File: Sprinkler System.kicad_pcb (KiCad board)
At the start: 2 copper layers, 165 x 85 mm, 74 parts, among them J1 Main Supply, J2 XFMR_Out, J20 Station_0, J21 Station_1, J22 Station_2, J23 Station_3, J24 Station_4, J25 Station_5, J3 XFMR_In, J4 Conn_Button, J5 UART0, J6 I2C, K1 G3MB-202P, K20 G5LE-1-DC5, K21 G5LE-1-DC5, K22 G5LE-1-DC5, K23 G5LE-1-DC5, K24 G5LE-1-DC5, K25 G5LE-1-DC5, SW1 EN, SW2 BOOT, U1 AMS1117-3.3, U2 EL817, U3 HLK-PM01, U4 ESP32-WROOM-32U, U5 ULN2803A

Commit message: Replace J1 mains connector with 5.08mm MSTBA (250V rated)
The previous Phoenix MC 1,5/3-G-3.81 connector is only rated 160V and
its 3.81mm pitch leaves just 2.0mm Live-to-Earth creepage at 240VAC.
Swap to MSTBA 2,5/3-G-5,08 (project-lib copy with silkscreen clipped at
the board edge), shift J1 up 2.5mm so the deeper body stays flush with
the edge, re-route the L_Supply/Neut/GND stubs, move the E/L/N labels
to the new pad pitch, and reshape the mains demarcation silk line and
the 24V_Comm corner to preserve >=3mm mains-to-SELV spacing.

ERC/DRC: 0 violations.

Co-Authored-By: Claude Fable 5 <noreply@anthropic.com>
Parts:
- J1: footprint Connector_Phoenix_MC:PhoenixContact_MC_1,5_3-G-3.81_1x03_P3.81mm_Horizontal -> Sprinkler System:PhoenixContact_MSTBA_2,5_3-G-5,08_1x03_P5.08mm_Horizontal_EdgeClip
- moved J1 2.50 mm to (82.0, 120.5)
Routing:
- net GND: track 132.1 -> 129.6 mm
- net L_Supply: track 26.7 -> 24.7 mm
- net Neut: track 56.3 -> 58.0 mm
- net 24V_Comm: track 237.0 -> 236.1 mm
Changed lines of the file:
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@@
 		)
 	)
-	(footprint "Connector_Phoenix_MC:PhoenixContact_MC_1,5_3-G-3.81_1x03_P3.81mm_Horizontal"
+	(footprint "Sprinkler System:PhoenixContact_MSTBA_2,5_3-G-5,08_1x03_P5.08mm_Horizontal_EdgeClip"
 		(layer "F.Cu")
-		(at 82 123)
-		(descr "Generic Phoenix Contact connector footprint for: MC_1,5/3-G-3.81; number of pins: 03; pin pitch: 3.81mm; Angled || order number: 1803280 8A 160V")
-		(tags "phoenix_contact connector MC_01x03_G_3.81mm")
+		(at 82 120.5)
+		(descr "Generic Phoenix Contact connector footprint for: MSTBA_2,5/3-G-5,08; number of pins: 03; pin pitch: 5.08mm; Angled || order number: 1757255 12A || order number: 1923872 16A (HC)")
+		(tags "phoenix_contact connector MSTBA_01x03_G_5.08mm")
 		(property "Reference" "J1"
-			(at 11.375 5.27 90)
+			(at -2.5 -4.3 0)
 			(layer "F.SilkS")
 			(effects
@@
 		)
 		(property "Value" "Main Supply"
-			(at -4.5 2.73 90)
-			(layer "F.SilkS")
+			(at 5.08 12.2 0)
+			(layer "F.Fab")
 			(effects
 				(font
@@
 		(duplicate_pad_numbers_are_jumpers no)
 		(fp_line
-			(start -2.71 -1.31)
-			(end -2.71 8.11)
+			(start -1 9.7)
+			(end 1 9.7)
+			(stroke
+				(width 0.12)
+				(type solid)
+			)
+			(layer "F.SilkS")
+		)
+		(fp_line
+			(start -0.75 8.61)
+			(end -1 9.7)
 			(stroke
 				(width 0.12)
@@
 		)
 		(fp_line
-			(start -2.71 -1.31)
-			(end -1.05 -1.31)
+			(start -0.3 -2.91)
+			(end 0.3 -2.91)
 			(stroke
 				(width 0.12)
@@
 		)
 		(fp_line
-			(start -2.71 4.8)
-			(end 10.33 4.8)
+			(start 0 -2.31)
+			(end -0.3 -2.91)
 			(stroke
 				(width 0.12)
@@
 		)
 		(fp_line
-			(start -2.71 8.11)
-			(end 10.33 8.11)
+			(start 0.3 -2.91)
+			(end 0 -2.31)
 			(stroke
 				(width 0.12)
@@
 		)
 		(fp_line
-			(start -0.3 -2.6)
-			(end 0.3 -2.6)
+			(start 0.75 8.61)
+			(end -0.75 8.61)
 			(stroke
 				(width 0.12)
@@
 		)
 		(fp_line
-			(start 0 -2)
-			(end -0.3 -2.6)
+			(start 1 9.7)
+			(end 0.75 8.61)
 			(stroke
 				(width 0.12)
@@
 		)
 		(fp_line
-			(start 0.3 -2.6)
-			(end 0 -2)
+			(start 4.08 9.7)
+			(end 6.08 9.7)
 			(stroke
 				(width 0.12)
@@
 		)
 		(fp_line
-			(start 1.05 -1.31)
-			(end 2.76 -1.31)
+			(start 4.33 8.61)
+			(end 4.08 9.7)
 			(stroke
 				(width 0.12)
@@
 		)
 		(fp_line
-			(start 4.86 -1.31)
-			(end 6.57 -1.31)
+			(start 5.83 8.61)
+			(end 4.33 8.61)
 			(stroke
 				(width 0.12)
@@
 		)
 		(fp_line
-			(start 10.33 -1.31)
-			(end 8.67 -1.31)
+			(start 6.08 9.7)
+			(end 5.83 8.61)
 			(stroke
 				(width 0.12)
@@
 		)
 		(fp_line
-			(start 10.33 8.11)
-			(end 10.33 -1.31)
+			(start 9.16 9.7)
+			(end 11.16 9.7)
+			(stroke
+				(width 0.12)
+				(type solid)
+			)
+			(layer "F.SilkS")
+		)
+		(fp_line
+			(start 9.41 8.61)
+			(end 9.16 9.7)
+			(stroke
+				(width 0.12)
+				(type solid)
+			)
+			(layer "F.SilkS")
+		)
+		(fp_line
+			(start 10.91 8.61)
+			(end 9.41 8.61)
+			(stroke
+				(width 0.12)
+				(type solid)
+			)
+			(layer "F.SilkS")
+		)
+		(fp_line
+			(start 11.16 9.7)
+			(end 10.91 8.61)
+			(stroke
+				(width 0.12)
+				(type solid)
+			)
+			(layer "F.SilkS")
+		)
+		(fp_rect
+			(start -3.65 -2.11)
+			(end 13.81 9.7)
 			(stroke
 				(width 0.12)
 				(type solid)
 			)
+			(fill no)
+			(layer "F.SilkS")
+		)
+		(fp_rect
+			(start -3.65 6.81)
+			(end 13.81 8.61)
+			(stroke
+				(width 0.12)
+				(type solid)
+			)
+			(fill no)
 			(layer "F.SilkS")
 		)
 		(fp_rect
-			(start -3.21 -2.3)
-			(end 10.72 8.5)
+			(start -4.04 -2.5)
+			(end 14.21 10.5)
 			(stroke
 				(width 0.05)
@@
 		)
 		(fp_line
-			(start 0 0)
-			(end -0.8 -1.2)
+			(start 0 -0.5)
+			(end -0.95 -2)
 			(stroke
 				(width 0.1)
@@
 		)
 		(fp_line
-			(start 0.8 -1.2)
-			(end 0 0)
+			(start 0.95 -2)
+			(end 0 -0.5)
 			(stroke
 				(width 0.1)
@@
 		)
 		(fp_rect
-			(start -2.6 -1.2)
-			(end 10.22 8)
+			(start -3.54 -2)
+			(end 13.7 10)
 			(stroke
 				(width 0.1)
@@
 		)
 		(fp_text user "${REFERENCE}"
-			(at 3.81 -0.5 0)
+			(at 5.08 -1.3 0)
 			(layer "F.Fab")
 			(effects
@@
 		(pad "1" thru_hole roundrect
 			(at 0 0)
-			(size 1.8 3.6)
-			(drill 1.2)
+			(size 2.08 3.6)
+			(drill 1.4)
 			(layers "*.Cu" "*.Mask")
 			(remove_unused_layers no)
-			(roundrect_rratio 0.138889)
+			(roundrect_rratio 0.120192)
 			(net "GND")
 			(pinfunction "Pin_1_1")
@@
 		)
 		(pad "2" thru_hole oval
-			(at 3.81 0)
-			(size 1.8 3.6)
-			(drill 1.2)
+			(at 5.08 0)
+			(size 2.08 3.6)
+			(drill 1.4)
 			(layers "*.Cu" "*.Mask")
 			(remove_unused_layers no)
@@
 		)
 		(pad "3" thru_hole oval
-			(at 7.62 0)
-			(size 1.8 3.6)
-			(drill 1.2)
+			(at 10.16 0)
+			(size 2.08 3.6)
+			(drill 1.4)
 			(layers "*.Cu" "*.Mask")
 			(remove_unused_layers no)
@@
 		)
 		(embedded_fonts no)
-		(model "${KICAD10_3DMODEL_DIR}/Connector_Phoenix_MC.3dshapes/PhoenixContact_MC_1,5_3-G-3.81_1x03_P3.81mm_Horizontal.step"
+		(model "${KICAD10_3DMODEL_DIR}/Connector_Phoenix_MSTB.3dshapes/PhoenixContact_MSTBA_2,5_3-G-5,08_1x03_P5.08mm_Horizontal.step"
 			(offset
 				(xyz 0 0 0)
@@
 		(property "Value" "EL817"
 			(at 0 3 0)
-			(layer "F.SilkS")
+			(layer "F.Fab")
 			(effects
 				(font
@@
 	(gr_line
 		(start 92.5 86.5)
-		(end 92.5 119.5)
+		(end 92.5 112)
 		(stroke
 			(width 0.2)
@@
 	)
 	(gr_line
-		(start 92.5 119.5)
-		(end 94.5 121)
+		(start 92.5 112)
+		(end 95.3 114.8)
 		(stroke
 			(width 0.2)
@@
 	)
 	(gr_line
-		(start 94.5 121)
-		(end 94.5 130)
+		(start 95.3 117.4)
+		(end 96.8 117.9)
+		(stroke
+			(width 0.2)
+			(type dash)
+		)
+		(layer "F.SilkS")
+	)
+	(gr_line
+		(start 96.8 117.9)
+		(end 96.8 130)
+		(stroke
+			(width 0.2)
+			(type dash)
+		)
+		(layer "F.SilkS")
+	)
+	(gr_line
+		(start 95.3 114.8)
+		(end 95.3 117.4)
 		(stroke
 			(width 0.2)
@@
 	)
 	(gr_text "E"
-		(at 81.28 120 0)
+		(at 82 117.5 0)
 		(layer "F.SilkS")
 		(effects
@@
 	)
 	(gr_text "L"
-		(at 85.09 120.65 0)
+		(at 87.08 117.5 0)
 		(layer "F.SilkS")
 		(effects
@@
 	)
 	(gr_text "N"
-		(at 89 120.5 0)
+		(at 92.16 117.5 0)
 		(layer "F.SilkS")
 		(effects
@@
 	(segment
 		(start 185 119)
-		(end 97 119)
+		(end 98.5 119)
 		(width 0.6)
 		(layer "B.Cu")
@@
 	)
 	(segment
-		(start 97 119)
-		(end 93 115)
+		(start 98.5 119)
+		(end 93 113.5)
 		(width 0.6)
 		(layer "B.Cu")
@@
 	)
 	(segment
-		(start 93 115)
+		(start 93 113.5)
 		(end 93 85)
 		(width 0.6)
@@
 	(segment
 		(start 82 112)
-		(end 82 123)
+		(end 82 120.5)
 		(width 0.5)
 		(layer "B.Cu")
@@
 	)
 	(segment
-		(start 89.59 122.7975)
-		(end 89.59 118.09)
+		(start 92.16 120.5)
+		(end 92.16 115.57)
 		(width 1)
 		(layer "F.Cu")
@@
 	)
 	(segment
-		(start 89.59 118.09)
-		(end 84.5 113)
+		(start 92.16 115.57)
+		(end 89.59 113)
 		(width 1)
 		(layer "F.Cu")
@@
 	(segment
 		(start 84 116.5)
-		(end 85.81 118.31)
+		(end 87.08 119.58)
 		(width 1)
 		(layer "F.Cu")
@@
 	)
 	(segment
-		(start 85.81 118.31)
-		(end 85.81 123)
+		(start 87.08 119.58)
+		(end 87.08 120.5)
 		(width 1)
 		(layer "F.Cu")
@@
 	)
 	(segment
-		(start 85.78 122.7975)
-		(end 85.7675 122.785)
-		(width 1)
-		(layer "B.Cu")
-		(net "L_Supply")
-	)
-	(segment
 		(start 71 107)
 		(end 71 109.3)
@@
 	)
 	(segment
+		(start 89.59 113)
+		(end 84.5 113)
+		(width 1)
+		(layer "F.Cu")
+		(net "Neut")
+	)
+	(segment

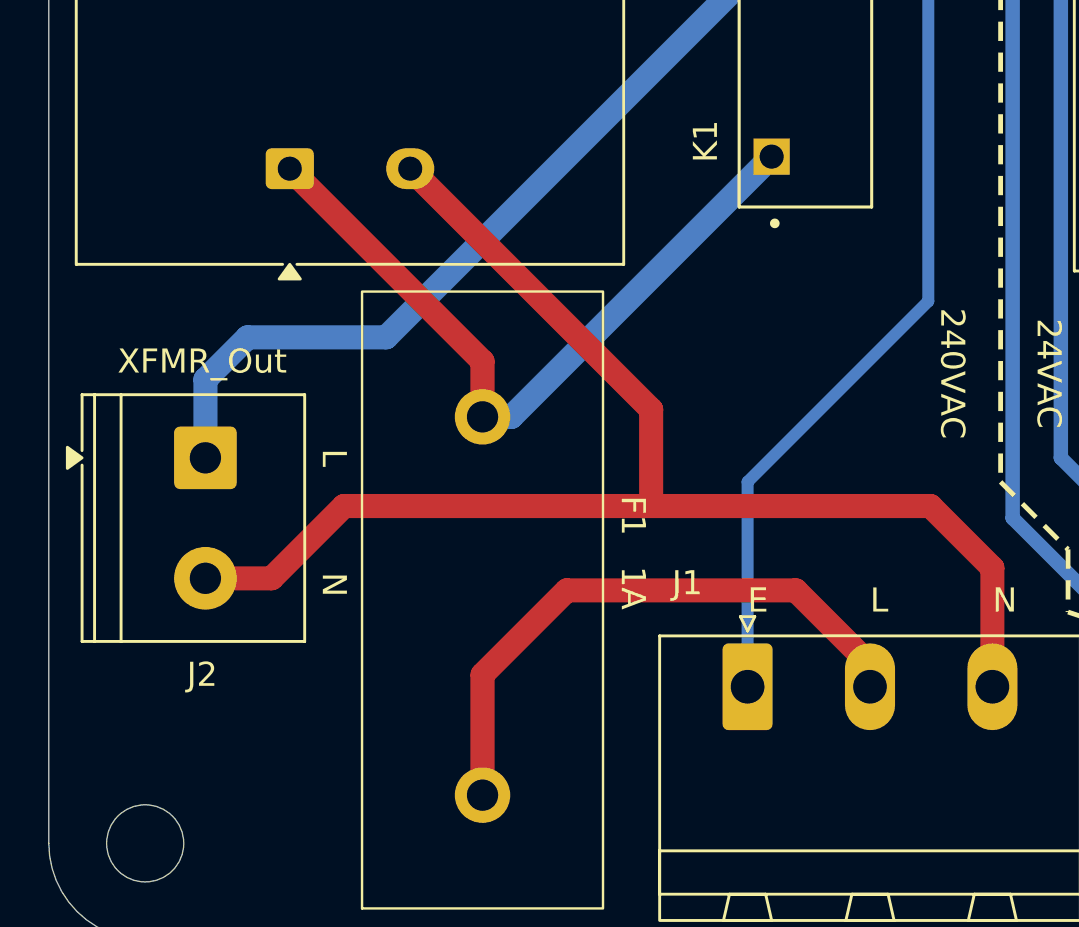
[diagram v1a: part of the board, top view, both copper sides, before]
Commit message: Add 10D471K MOVs: RV1 across transformer primary, RV2 across mains input
The G3MB-202P SSR has a built-in snubber but no overvoltage element;
Omron requires external overvoltage protection for inductive loads.
RV1 (L_SW-Neut) clamps the transformer-primary inductive kick at J2;
RV2 (L-Neut, after F1) provides the HLK-PM01 datasheet-recommended
line surge protection.

Layout: J2 moved up 4.5mm to open space for RV1 below it (clear of the
H3 mounting hole), earth track jogged from x82 to x82.5 to keep >=3mm
from RV2's Neutral pad, J2's L/N silk labels and Reference/Value moved
with it, F1 reference relocated out of RV2's outline. RV1 uses a
project-library footprint copy with silk clipped at the left to clear
the board-margin line.

ERC/DRC: 0 violations. Mains-to-SELV spacing verified >=3mm.

Co-Authored-By: Claude Fable 5 <noreply@anthropic.com>
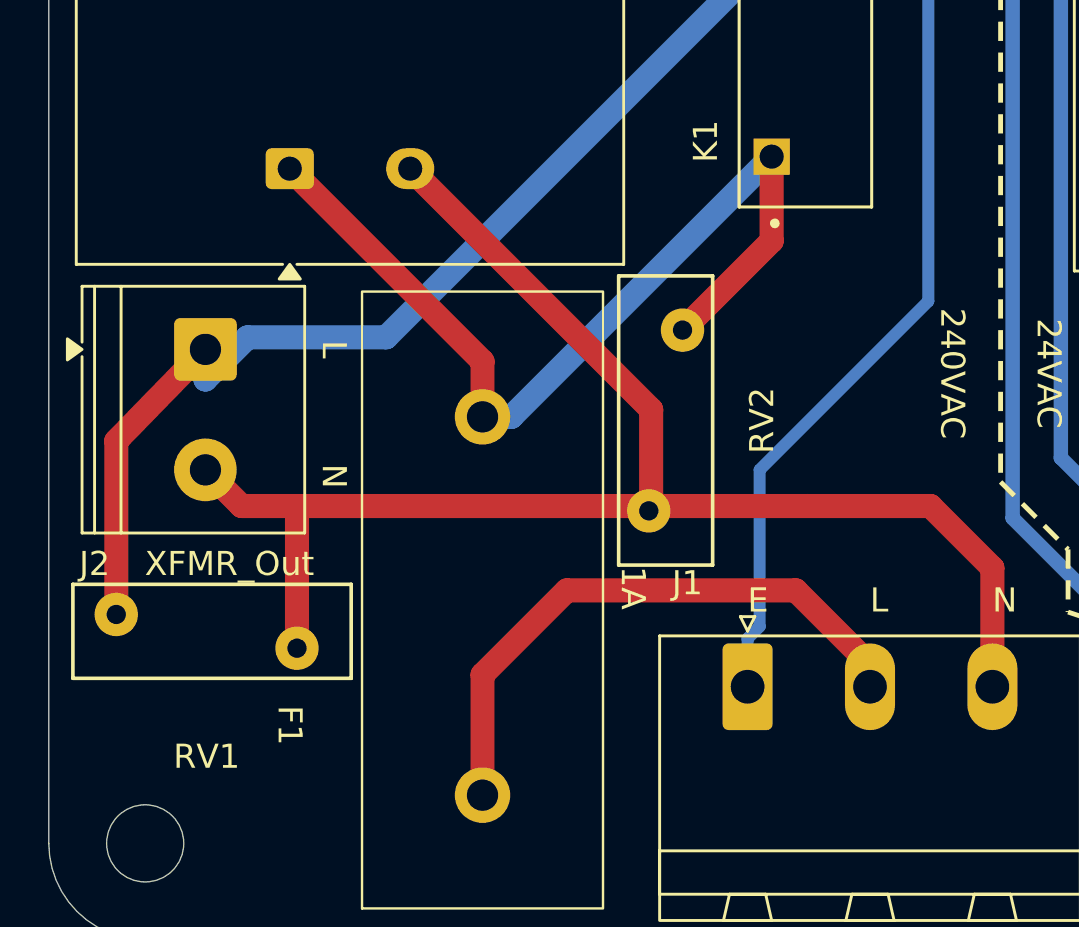
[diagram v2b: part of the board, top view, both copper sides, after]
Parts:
- added RV1: 10D471K, Sprinkler System:RV_Disc_D12mm_W3.9mm_P7.5mm_EdgeClip, F.Cu at (55.8, 117.5)
- added RV2: 10D471K, Varistor:RV_Disc_D12mm_W3.9mm_P7.5mm, F.Cu at (79.3, 105.7)
- moved J2 4.50 mm to (59.5, 106.5)
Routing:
- net L_SW: track 33.7 -> 44.2 mm
- net L: track 30.1 -> 38.8 mm
- net Neut: track 58.0 -> 63.5 mm

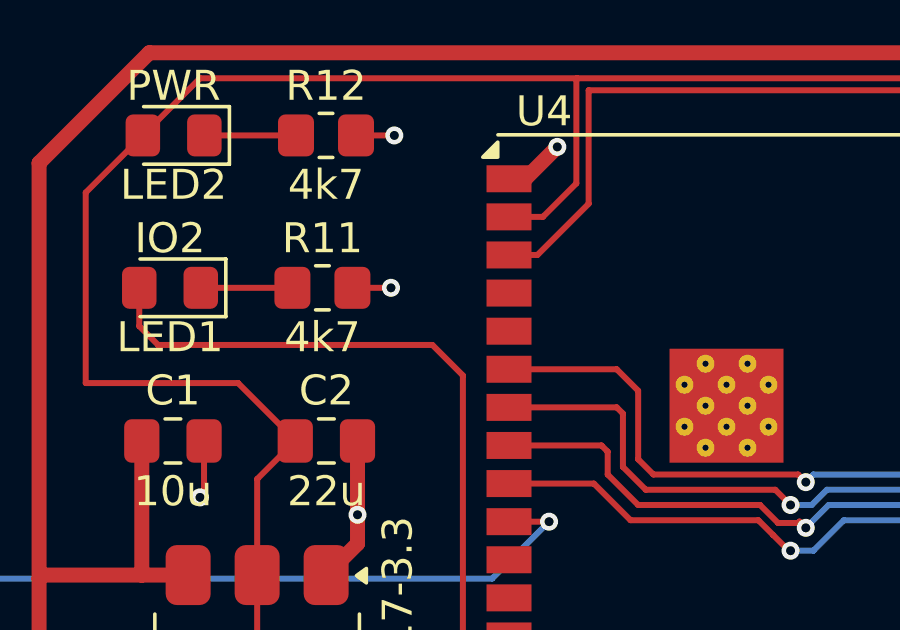
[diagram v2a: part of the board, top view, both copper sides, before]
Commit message: Add C5 100nF reset capacitor on ESP32 EN
Espressif's reference design calls for an RC delay on EN (R3 10k was
already present, the capacitor was missing) to guarantee clean power-on
reset as the 3V3 rail rises. Placed beside U4's EN pin, grounded via
the existing GND via at (134.4, 57.8). Also debounces SW1.

ERC/DRC: 0 violations.

Co-Authored-By: Claude Fable 5 <noreply@anthropic.com>
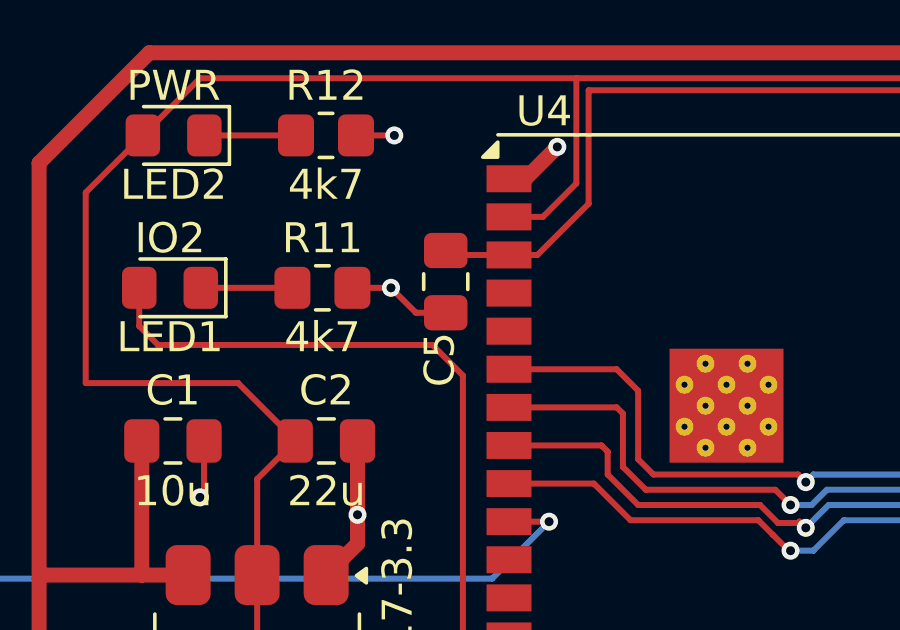
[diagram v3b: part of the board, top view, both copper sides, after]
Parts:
- added C5: 100n, Capacitor_SMD:C_0805_2012Metric_Pad1.18x1.45mm_HandSolder, F.Cu at (136.1, 57.6)
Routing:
- net GND: track 129.6 -> 131.7 mm
- net /EN: track 37.6 -> 39.7 mm
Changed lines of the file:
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@@
 		)
 	)
+	(footprint "Capacitor_SMD:C_0805_2012Metric_Pad1.18x1.45mm_HandSolder"
+		(layer "F.Cu")
+		(at 136.1 57.6 90)
+		(descr "Capacitor SMD 0805 (2012 Metric), square (rectangular) end terminal, IPC-7351 nominal with elongated pad for handsoldering. (Body size source: IPC-SM-782 page 76, https://www.pcb-3d.com/wordpress/wp-content/uploads/ipc-sm-782a_amendment_1_and_2.pdf, https://docs.google.com/spreadsheets/d/1BsfQQcO9C6DZCsRaXUlFlo91Tg2WpOkGARC1WS5S8t0/edit?usp=sharing)")
+		(tags "capacitor handsolder")
+		(property "Reference" "C5"
+			(at -2.6 -0.1975 270)
+			(layer "F.SilkS")
+			(effects
+				(font
+					(size 1 1)
+					(thickness 0.15)
+				)
+			)
+		)
+		(property "Value" "100n"
+			(at -2.8725 -0.1975 270)
+			(layer "F.Fab")
+			(effects
+				(font
+					(size 1 1)
+					(thickness 0.15)
+				)
+			)
+		)
+		(property "Datasheet" ""
+			(at 0 0 0)
+			(layer "F.Fab")
+			(hide yes)
+			(effects
+				(font
+					(size 1.27 1.27)
+				)
+			)
+		)
+		(property "Description" "Unpolarized capacitor"
+			(at 0 0 0)
+			(layer "F.Fab")
+			(hide yes)
+			(effects
+				(font
+					(size 1.27 1.27)
+				)
+			)
+		)
+		(property "KiLib_Generator" "SMD_2terminal_chip_molded"
+			(at 0 0 0)
+			(layer "F.SilkS")
+			(hide yes)
+			(effects
+				(font
+					(size 1 1)
+					(thickness 0.15)
+				)
+			)
+		)
+		(property ki_fp_filters "C_*")
+		(sheetname "/")
+		(sheetfile "Sprinkler System.kicad_sch")
+		(units
+			(unit
+				(name "A")
+				(pins "1" "2")
+			)
+		)
+		(attr smd)
+		(duplicate_pad_numbers_are_jumpers no)
+		(fp_line
+			(start -0.261252 -0.735)
+			(end 0.261252 -0.735)
+			(stroke
+				(width 0.12)
+				(type solid)
+			)
+			(layer "F.SilkS")
+		)
+		(fp_line
+			(start -0.261252 0.735)
+			(end 0.261252 0.735)
+			(stroke
+				(width 0.12)
+				(type solid)
+			)
+			(layer "F.SilkS")
+		)
+		(fp_rect
+			(start -1.88 -0.98)
+			(end 1.88 0.98)
+			(stroke
+				(width 0.05)
+				(type solid)
+			)
+			(fill no)
+			(layer "F.CrtYd")
+		)
+		(fp_rect
+			(start -1 -0.625)
+			(end 1 0.625)
+			(stroke
+				(width 0.1)
+				(type solid)
+			)
+			(fill no)
+			(layer "F.Fab")
+		)
+		(fp_text user "${REFERENCE}"
+			(at 0 0 0)
+			(layer "F.Fab")
+			(effects
+				(font
+					(size 0.5 0.5)
+					(thickness 0.08)
+				)
+			)
+		)
+		(pad "1" smd roundrect
+			(at -1.0375 0 90)
+			(size 1.175 1.45)
+			(layers "F.Cu" "F.Mask" "F.Paste")
+			(roundrect_rratio 0.212766)
+			(net "GND")
+			(pintype "passive")
+		)
+		(pad "2" smd roundrect
+			(at 1.0375 0 90)
+			(size 1.175 1.45)
+			(layers "F.Cu" "F.Mask" "F.Paste")
+			(roundrect_rratio 0.212766)
+			(net "/EN")
+			(pintype "passive")
+		)
+		(embedded_fonts no)
+		(model "${KICAD10_3DMODEL_DIR}/Capacitor_SMD.3dshapes/C_0805_2012Metric.step"
+			(offset
+				(xyz 0 0 0)
+			)
+			(scale
+				(xyz 1 1 1)
+			)
+			(rotate
+				(xyz 0 0 0)
+			)
+		)
+	)
 	(footprint "Varistor:RV_Disc_D15.5mm_W5.4mm_P7.5mm"
 		(layer "F.Cu")
@@
 		(net "GND")
 	)
+	(segment
+		(start 136.1 56.7115)
+		(end 138.2095 56.7115)
+		(width 0.2)
+		(layer "F.Cu")
+		(net "/EN")
+	)
+	(segment
+		(start 136.1 58.6375)
+		(end 135.1065 58.6375)
+		(width 0.2)
+		(layer "F.Cu")
+		(net "GND")
+	)
+	(segment
+		(start 135.1065 58.6375)
+		(end 134.2755 57.8065)
+		(width 0.2)
+		(layer "F.Cu")
+		(net "GND")
+	)

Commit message: Add C6 100nF at ESP32 VDD and C7 220uF bulk on the 5V rail
The HLK-PM01 is rated 600mA and ESP32 WiFi TX bursts approach 500mA;
the 5V rail previously had only 10uF of bulk. C7 (220uF radial, THT
D6.3/P2.5) sits above U3 tapping the +5V/GND module pins on B.Cu with
a via to the existing front-side GND run. C6 gives U4 local 3V3
decoupling next to its VDD pin (none existed within 20mm).

The planned third 100nF at U5 was dropped: every approach to the
ULN2803A's COM/GND pins is walled by the zone-driver fan-out on both
layers, and the ULN has no supply pin proper - the flyback return path
through the 5V artery is already served by C7.

ERC/DRC: 0 violations.

Co-Authored-By: Claude Fable 5 <noreply@anthropic.com>
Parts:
- added C6: 100n, Capacitor_SMD:C_0805_2012Metric_Pad1.18x1.45mm_HandSolder, F.Cu at (136.1, 53.5)
- added C7: 220u, Capacitor_THT:CP_Radial_D6.3mm_P2.50mm, F.Cu at (74.5, 60.0)
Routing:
- net GND: track 131.7 -> 148.6 mm, vias 16 -> 17
- net +5V: track 308.3 -> 319.5 mm
- net +3V3: track 176.5 -> 178.9 mm

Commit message: Add D2 back-feed blocking diode for the UART/I2C 5V branch (DNP)
SS34 Schottky (SMA, back side) inline in the 5V rail between the main
supply and the J5/J6 connector branch, so an external USB-UART adapter
on J5 can power the board but the HLK-PM01 can never back-drive the
adapter. Marked DNP: bridge the pads (back-side silk note) until a
Schottky is sourced - a plain silicon diode drops too much for the
AMS1117's headroom and must not be substituted.

The branch becomes net +5V_UART (J5 pin 2 and, until the I2C supply
jumper lands in the next change, J6 pin 2). Zones refilled via
kicad-cli --refill-zones.

ERC/DRC: 0 violations.

Co-Authored-By: Claude Fable 5 <noreply@anthropic.com>
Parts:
- added D2: SS34, D_SMA, B.Cu at (170.0, 50.0)
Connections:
- J5 pad 2: +5V -> /+5V_UART
- J6 pad 2: +5V -> /+5V_UART
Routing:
- net +5V: track 319.5 -> 291.1 mm
- net /+5V_UART: track 0.00 -> 24.4 mm, vias 0 -> 2
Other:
- board text added: "D2: SS34 or bridge"
